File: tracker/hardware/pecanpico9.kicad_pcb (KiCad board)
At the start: 2 copper layers, 29.8 x 33.7 mm, 116 parts, among them IC1 SPV1040T, IC2 TPS62260DRVR, IC3 ADP322ACPZ-115-R7, IC4 Si4063-B1B-FM, IC5 STM32F413xG, IC6 EVA-7M, IC7 PAC1720-1-AIA-TR, IC8 LDLN015PU33R, IC9 BME280, P1 CONN_01X25, P2 CONN_01X10, P3 ZX62-B-5PA(33), P4 IPX 2mm, P5 CONN_01X02, P6 IPX 2mm, Q1 FDN306P, X1 KT2016K26000BCW18ZAS

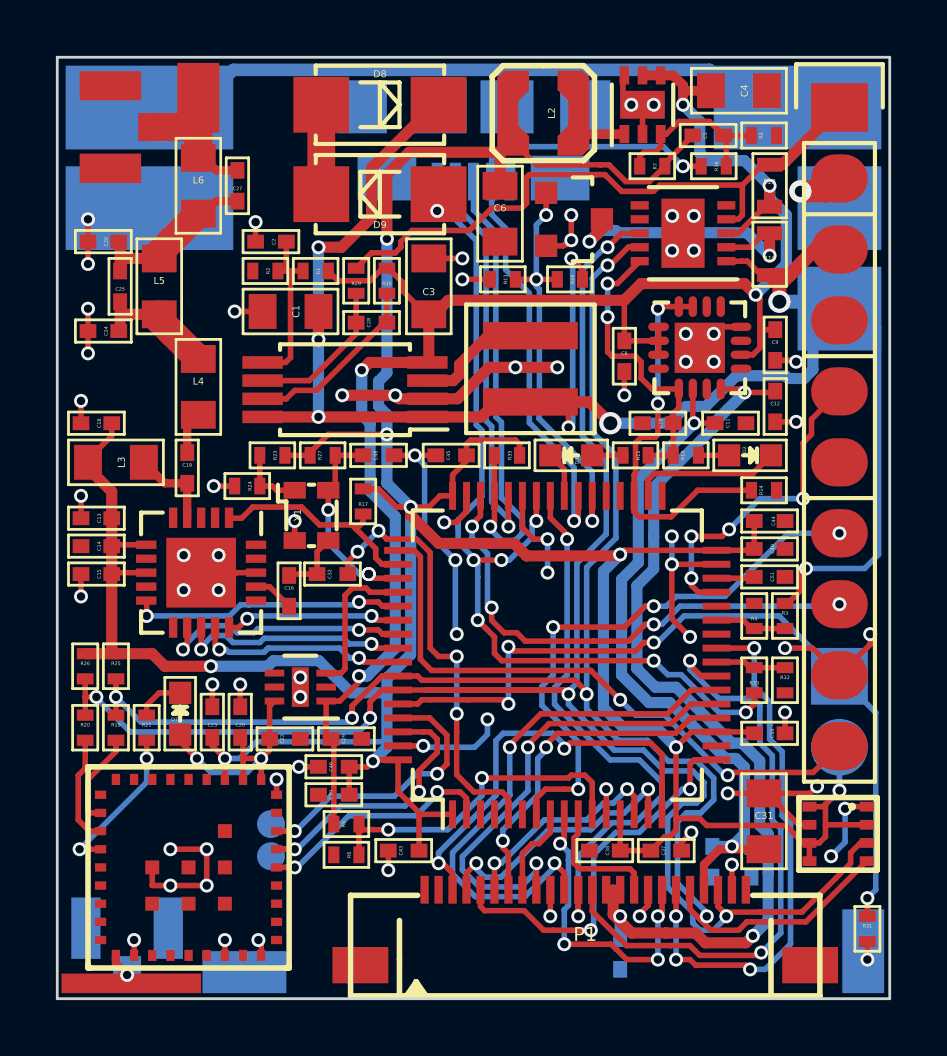
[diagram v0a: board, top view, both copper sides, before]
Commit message: Fixed SOT-23 footprint (wrong numbering) Moved LEDs (so they are not too close to the very big inductor) Added Pulldown to GPS_EN
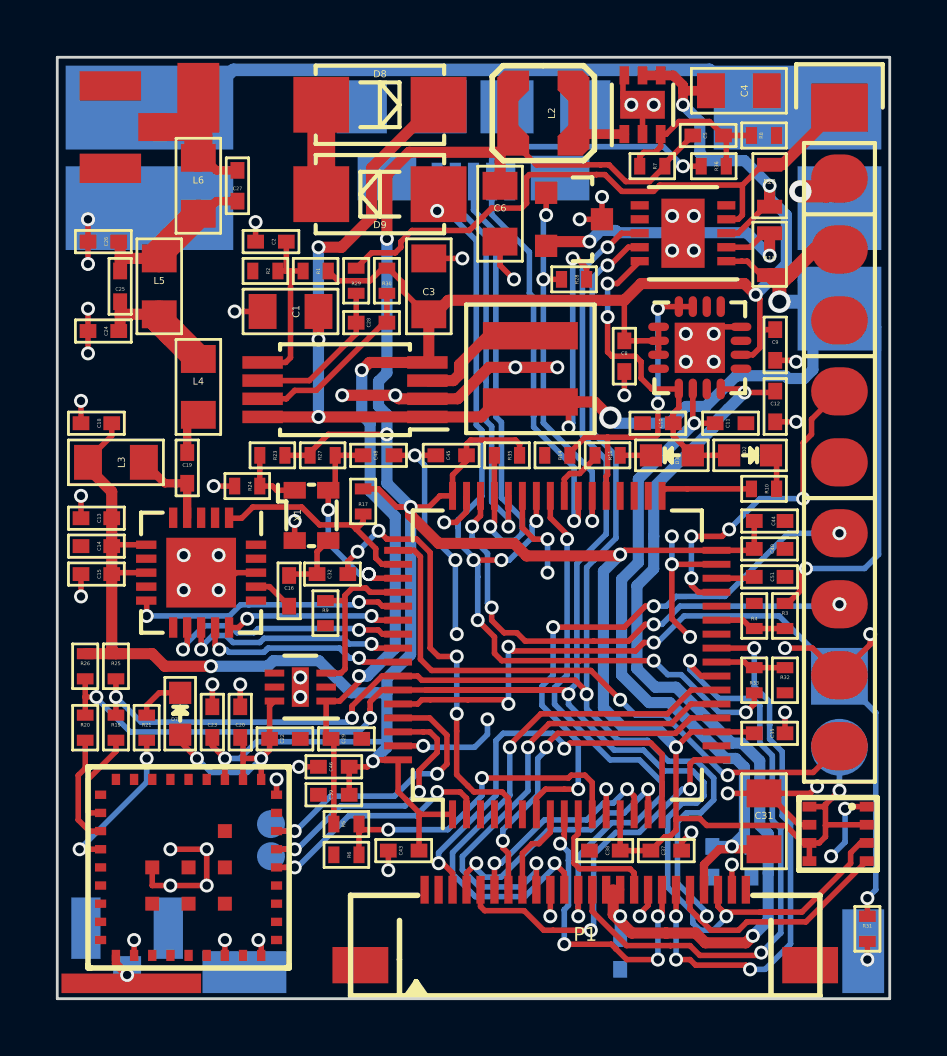
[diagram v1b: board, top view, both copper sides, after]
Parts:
- removed R13: N/A, stm32f7:R_0402
- added R9: 100k, stm32f7:R_0402, F.Cu at (56.7, 110.8)
- C25, C27: value 470p -> 3.3p
- Q1: footprint TO_SOT_Packages_SMD:SOT-23 -> stm32f7:SOT-23
- moved R14 7.50 mm to (65.0, 105.2), turned to 180 degrees
- moved D3 3.60 mm to (69.1, 105.2)
- moved R10 3.05 mm to (72.4, 106.3), turned to 180 degrees
- moved R11 1.00 mm to (66.8, 105.2)
- moved R28 0.15 mm to (65.6, 98.8)
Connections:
- D2 pad 1: /IO_LED2 -> Net-(D2-Pad1)
- D2 pad 2: Net-(D2-Pad2) -> +3V3
- D3 pad 1: /IO_LED3 -> Net-(D3-Pad1)
- D3 pad 2: Net-(D3-Pad2) -> +3V3
- IC5 pad 33: (no net) -> /IO_LED2
- IC5 pad 34: /IO_LED2 -> (no net)
- IC5 pad 35: /CAM_EN -> (no net)
- IC5 pad 37: (no net) -> /CAM_EN
- R10 pad 1: +3V3 -> Net-(D2-Pad1)
- R10 pad 2: Net-(D2-Pad2) -> /IO_LED2
- R11 pad 1: +3V3 -> Net-(D3-Pad1)
- R11 pad 2: Net-(D3-Pad2) -> /IO_LED3
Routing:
- net /CAM_EN: track 13.9 -> 11.4 mm
- net /IO_LED2: track 5.34 -> 3.39 mm
- net Net-(D2-Pad1): track 0.00 -> 1.28 mm
- net Net-(D3-Pad2): track 1.25 -> 0.00 mm
- net Net-(D3-Pad1): track 0.00 -> 1.10 mm
- net Net-(D2-Pad2): track 1.10 -> 0.00 mm
- net /SOL_SHORT_EN: track 15.1 -> 14.1 mm
- net /GPS_EN: track 5.44 -> 6.15 mm
- net /SENSE_SOL-: track 10.5 -> 11.2 mm
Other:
- net class Default: trace_width 0.4 -> 0.2

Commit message: Removed OSC+ net and salvaging pin for Si4464 Changed a lot of STM32 connections
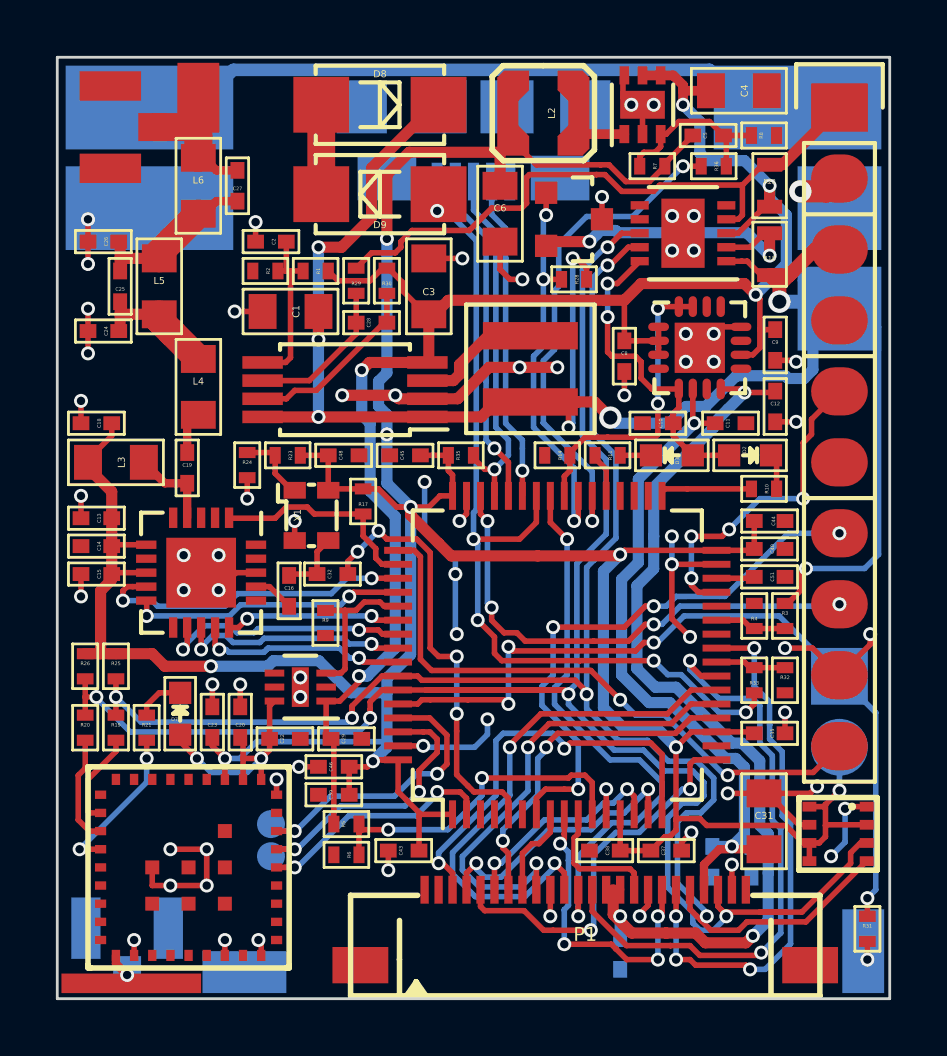
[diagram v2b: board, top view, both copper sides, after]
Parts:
- removed R27: 0R, stm32f7:R_0402
- moved C45 1.65 mm to (59.5, 105.2)
- moved R35 1.65 mm to (61.5, 105.2), turned to 0 degrees
- moved C48 1.25 mm to (57.4, 105.2)
- moved R24 0.75 mm to (53.9, 105.5), turned to 270 degrees
- moved R23 0.55 mm to (55.4, 105.2)
- moved R9 0.35 mm to (56.7, 111.2)
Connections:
- C48 pad 1: +OSC -> +1V8
- IC4 pad 9: (no net) -> /RADIO_GPIO0
- IC5 pad 37: /CAM_EN -> /IO_LED3
- IC5 pad 38: /SOL_SHORT_EN -> /V_BOOST
- IC5 pad 39: /V_BOOST -> /SOL_SHORT_EN
- IC5 pad 40: /IO_LED3 -> /CAM_EN
- IC5 pad 43: GND -> /USB_ID
- IC5 pad 51: +OSC -> /RADIO_GPIO0
- IC5 pad 52: /GPS_EN -> /RADIO_GPIO1
- IC5 pad 53: /RADIO_GPIO1 -> /GPS_EN
- P3 pad 4: /V_BOOST -> /USB_ID
- X1 pad 4: +OSC -> +1V8
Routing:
- net GND: track 87.2 -> 74.4 mm, vias 74 -> 68
- net /USB_ID: track 0.00 -> 12.4 mm, vias 0 -> 1
- net /RADIO_GPIO0: track 0.00 -> 11.6 mm, vias 0 -> 2
- net +OSC: track 7.26 -> 0.00 mm, vias 3 -> 0
- net (no net): track 0.00 -> 5.93 mm, vias 0 -> 3
- net /V_BOOST: track 23.8 -> 18.0 mm
- net /USB_D+: track 17.4 -> 13.0 mm
- net +1V8: track 132.1 -> 129.6 mm
- net /USB_D-: track 14.2 -> 12.0 mm
- net /USB_VUSB: track 33.5 -> 32.2 mm, vias 7 -> 5
- net /CAM_EN: track 11.4 -> 10.8 mm
- net /GPS_EN: track 6.15 -> 5.62 mm

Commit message: Removed I2C 0R resistors, removed USB diodes, Added USB ID
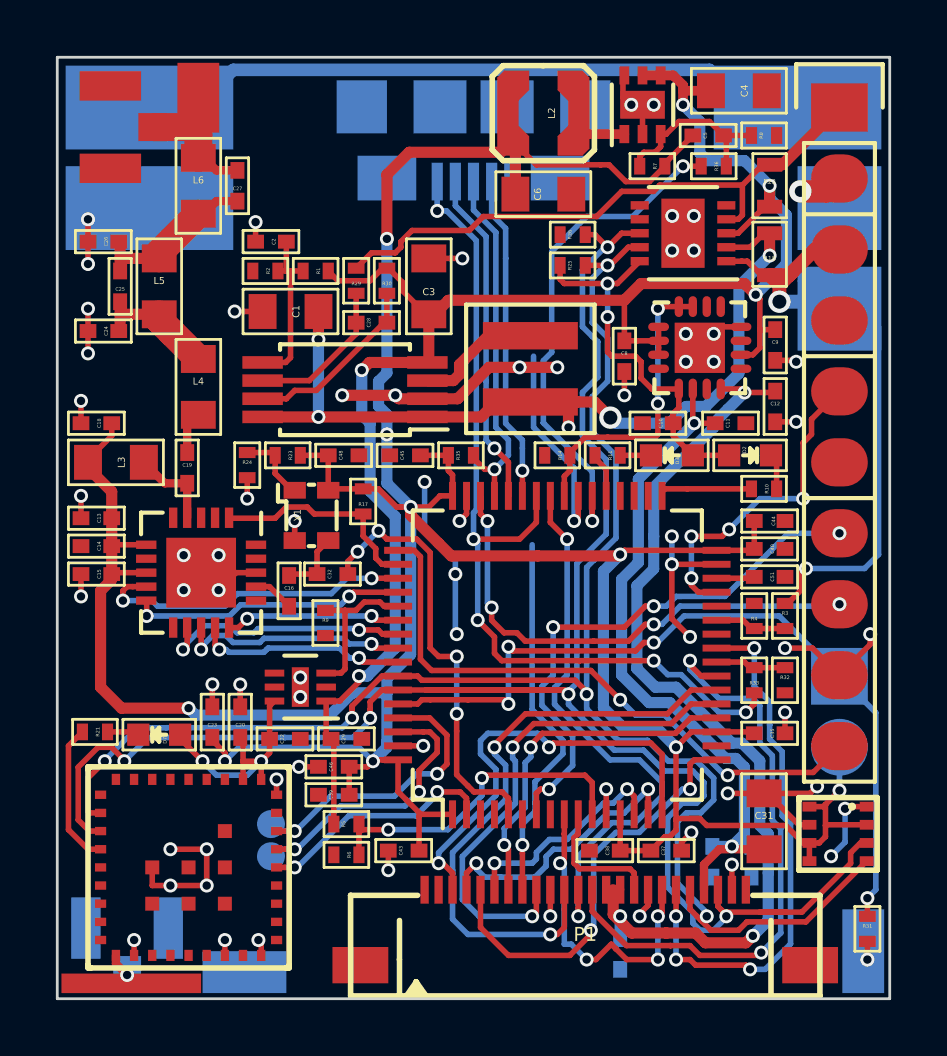
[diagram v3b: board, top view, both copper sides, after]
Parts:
- removed D8, D9: RFN1L7STE25, stm32f7:RFN1L7S
- removed Q1: FDN306P, stm32f7:SOT-23
- removed R19, R20: N/A, stm32f7:R_0402
- removed R28: 100k, stm32f7:R_0402
- moved R26 23.3 mm to (65.5, 97.2), turned to 0 degrees
- moved R25 21.8 mm to (65.5, 98.3), turned to 0 degrees
- moved R21 1.86 mm to (48.5, 115.0), turned to 180 degrees
- moved C6 1.70 mm to (64.5, 95.8), turned to 0 degrees
- moved D7 1.06 mm to (50.8, 115.2), turned to 0 degrees
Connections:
- C1 pad 1: +SOL -> /SENSE_SOL
- IC1 pad 1: +SOL -> /SENSE_SOL
- IC1 pad 8: +SOL -> /SENSE_SOL
- IC5 pad 10: /CAM_HREF -> (no net)
- IC5 pad 36: (no net) -> /IO_LED3
- IC5 pad 37: /IO_LED3 -> /CAM_PCLK
- IC5 pad 39: /SOL_SHORT_EN -> (no net)
- IC5 pad 8: /CAM_PCLK -> (no net)
- IC6 pad 29: Net-(IC6-Pad29) -> /I2C_SCL
- IC6 pad 30: Net-(IC6-Pad30) -> /I2C_SDA
- IC7 pad 2: /SENSE_SOL- -> /SENSE_SOL
- L1 pad 2: +SOL -> /SENSE_SOL
- P1 pad 16: /CAM_HREF -> (no net)
- R18 pad 2: /SENSE_SOL- -> /SENSE_SOL
- R25 pad 1: +1V8 -> +3V3
- R26 pad 1: +1V8 -> +3V3
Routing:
- net +SOL: track 72.6 -> 26.3 mm, vias 8 -> 2
- net /SENSE_SOL: track 0.00 -> 31.6 mm, vias 0 -> 5
- net /SOL_SHORT_EN: track 14.1 -> 0.00 mm, vias 3 -> 0
- net (no net): track 5.93 -> 18.1 mm, vias 3 -> 4
- net /SENSE_SOL-: track 11.2 -> 0.00 mm, vias 2 -> 0
- net /CAM_PCLK: track 3.26 -> 14.4 mm, vias 0 -> 1
- net GND: track 74.4 -> 68.7 mm, vias 68 -> 65
- net /CAM_HREF: track 4.71 -> 0.00 mm
- net Net-(IC6-Pad30): track 3.92 -> 0.00 mm
- net /I2C_SDA: track 67.1 -> 70.8 mm
- net Net-(IC6-Pad29): track 3.43 -> 0.00 mm
- net Net-(D8-Pad2): track 3.20 -> 0.00 mm
- net /I2C_SCL: track 58.8 -> 61.9 mm
- net /CAM_D8: track 19.3 -> 21.8 mm
- net +3V3: track 11.4 -> 13.7 mm
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
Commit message: Reverted post hardware changes to produced version There was the plan to create Pecan Pico 9b, but all those changes have been put into Pecan Pico 10a.
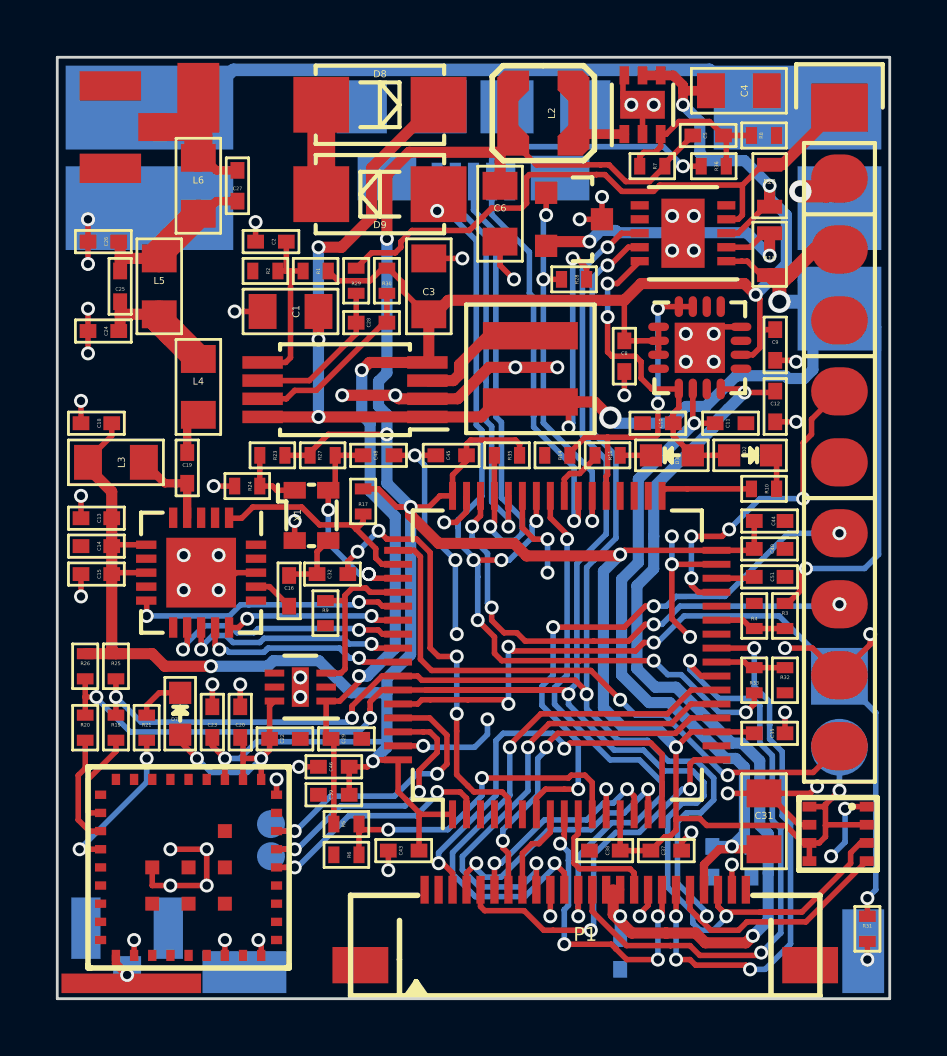
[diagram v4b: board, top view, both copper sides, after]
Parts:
- added D8: RFN1L7STE25, stm32f7:RFN1L7S, F.Cu at (58.6, 92.6)
- added D9: RFN1L7STE25, stm32f7:RFN1L7S, F.Cu at (58.6, 95.8)
- added Q1: FDN306P, stm32f7:SOT-23, F.Cu at (65.6, 96.7)
- added R19: N/A, stm32f7:R_0402, F.Cu at (49.2, 114.9)
- added R20: N/A, stm32f7:R_0402, F.Cu at (48.1, 114.9)
- added R27: 0R, stm32f7:R_0402, F.Cu at (56.6, 105.2)
- added R28: 100k, stm32f7:R_0402, F.Cu at (65.6, 98.8)
- moved R26 23.3 mm to (48.1, 112.7), turned to 270 degrees
- moved R25 21.8 mm to (49.2, 112.7), turned to 270 degrees
- moved R21 1.86 mm to (50.3, 114.9), turned to 270 degrees
- moved C6 1.70 mm to (63.0, 96.5), turned to 270 degrees
- moved C45 1.65 mm to (61.2, 105.2)
- moved R35 1.65 mm to (63.2, 105.2), turned to 180 degrees
- moved C48 1.25 mm to (58.6, 105.2)
- moved D7 1.06 mm to (51.5, 114.4), turned to 270 degrees
- moved R24 0.75 mm to (53.9, 106.2), turned to 180 degrees
- moved R23 0.55 mm to (54.8, 105.2)
- moved R9 0.35 mm to (56.7, 110.8)
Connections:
- C1 pad 1: /SENSE_SOL -> +SOL
- C48 pad 1: +1V8 -> +OSC
- IC1 pad 1: /SENSE_SOL -> +SOL
- IC1 pad 8: /SENSE_SOL -> +SOL
- IC4 pad 9: /RADIO_GPIO0 -> (no net)
- IC5 pad 10: (no net) -> /CAM_HREF
- IC5 pad 36: /IO_LED3 -> (no net)
- IC5 pad 37: /CAM_PCLK -> /CAM_EN
- IC5 pad 38: /V_BOOST -> /SOL_SHORT_EN
- IC5 pad 39: (no net) -> /V_BOOST
- IC5 pad 40: /CAM_EN -> /IO_LED3
- IC5 pad 43: /USB_ID -> GND
- IC5 pad 51: /RADIO_GPIO0 -> +OSC
- IC5 pad 52: /RADIO_GPIO1 -> /GPS_EN
- IC5 pad 53: /GPS_EN -> /RADIO_GPIO1
- IC5 pad 8: (no net) -> /CAM_PCLK
- IC6 pad 29: /I2C_SCL -> Net-(IC6-Pad29)
- IC6 pad 30: /I2C_SDA -> Net-(IC6-Pad30)
- IC7 pad 2: /SENSE_SOL -> /SENSE_SOL-
- L1 pad 2: /SENSE_SOL -> +SOL
- P1 pad 16: (no net) -> /CAM_HREF
- P3 pad 4: /USB_ID -> /V_BOOST
- R18 pad 2: /SENSE_SOL -> /SENSE_SOL-
- R25 pad 1: +3V3 -> +1V8
- R26 pad 1: +3V3 -> +1V8
- X1 pad 4: +1V8 -> +OSC
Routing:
- net +SOL: track 26.3 -> 72.6 mm, vias 2 -> 8
- net /SENSE_SOL: track 31.6 -> 0.00 mm, vias 5 -> 0
- net GND: track 68.7 -> 87.2 mm, vias 65 -> 74
- net (no net): track 18.1 -> 0.00 mm, vias 4 -> 0
- net /SOL_SHORT_EN: track 0.00 -> 14.1 mm, vias 0 -> 3
- net /USB_ID: track 12.4 -> 0.00 mm, vias 1 -> 0
- net /RADIO_GPIO0: track 11.6 -> 0.00 mm, vias 2 -> 0
- net /SENSE_SOL-: track 0.00 -> 11.2 mm, vias 0 -> 2
- net /CAM_PCLK: track 14.4 -> 3.26 mm, vias 1 -> 0
- net +OSC: track 0.00 -> 7.26 mm, vias 0 -> 3
- net /V_BOOST: track 18.0 -> 23.8 mm
- net /CAM_HREF: track 0.00 -> 4.71 mm
- net /USB_D+: track 13.0 -> 17.4 mm
- net Net-(IC6-Pad30): track 0.00 -> 3.92 mm
- net /I2C_SDA: track 70.8 -> 67.1 mm
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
